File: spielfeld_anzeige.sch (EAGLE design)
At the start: 22 parts, among them IC1 UDN2981A, IC2 UDN2981A, IC3 74HC595N, IC4 74HC595N, IC5 74HC595N

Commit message: Schematic mit 3 Digits fertig
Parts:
- removed R2: (no value), rcl:R-EU_R3216
- JP1: value (none) -> 8 Pin
- L1, L2: value (none) -> red
- R1: value (none) -> 56
- R3: value (none) -> 10k
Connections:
- removed net GND1: C1.2
- removed net GND2: C3.2
- removed net N$18: L2.A, R2.1
- removed net N$19: L1.A, R1.1
- net +5V: now also IC1.VS, IC2.VS; no longer IC1.GND, IC2.GND
- net COLON_OUT: now also IC2.O8, R1.2; no longer RN4D.2
- net GND: now also C1.2, C3.2, IC1.GND, IC2.GND; no longer IC1.VS, IC2.VS, L2.C
- net N$1: now also L1.A, L2.C; no longer ICL1.O1
- net N$13: now also L2.A, R1.1; no longer IC2.O8, RN4D.1
- net R1_OUT: now also D2.R1, D3.R1, ICL1.O1
- net R2_OUT: now also D2.R2, D3.R2, ICL1.O2
- net R3_OUT: now also D2.R3, D3.R3, ICL1.O3
- net R4_OUT: now also D2.R4, D2.R4@1, D3.R4, D3.R4@1, ICL1.O4
- net R5_OUT: now also D2.R5, D3.R5, ICL1.O5
- net R6_OUT: now also D2.R6, D3.R6, ICL1.O6
- net R7_OUT: now also D2.R7, D3.R7, ICL1.O7
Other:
- note added: "Board Connector"
- note added: "Shift-Reg Clear"
- note removed: "Connector"
- moved on the sheet: JP1, L1, L2, R1, R3, RN4D

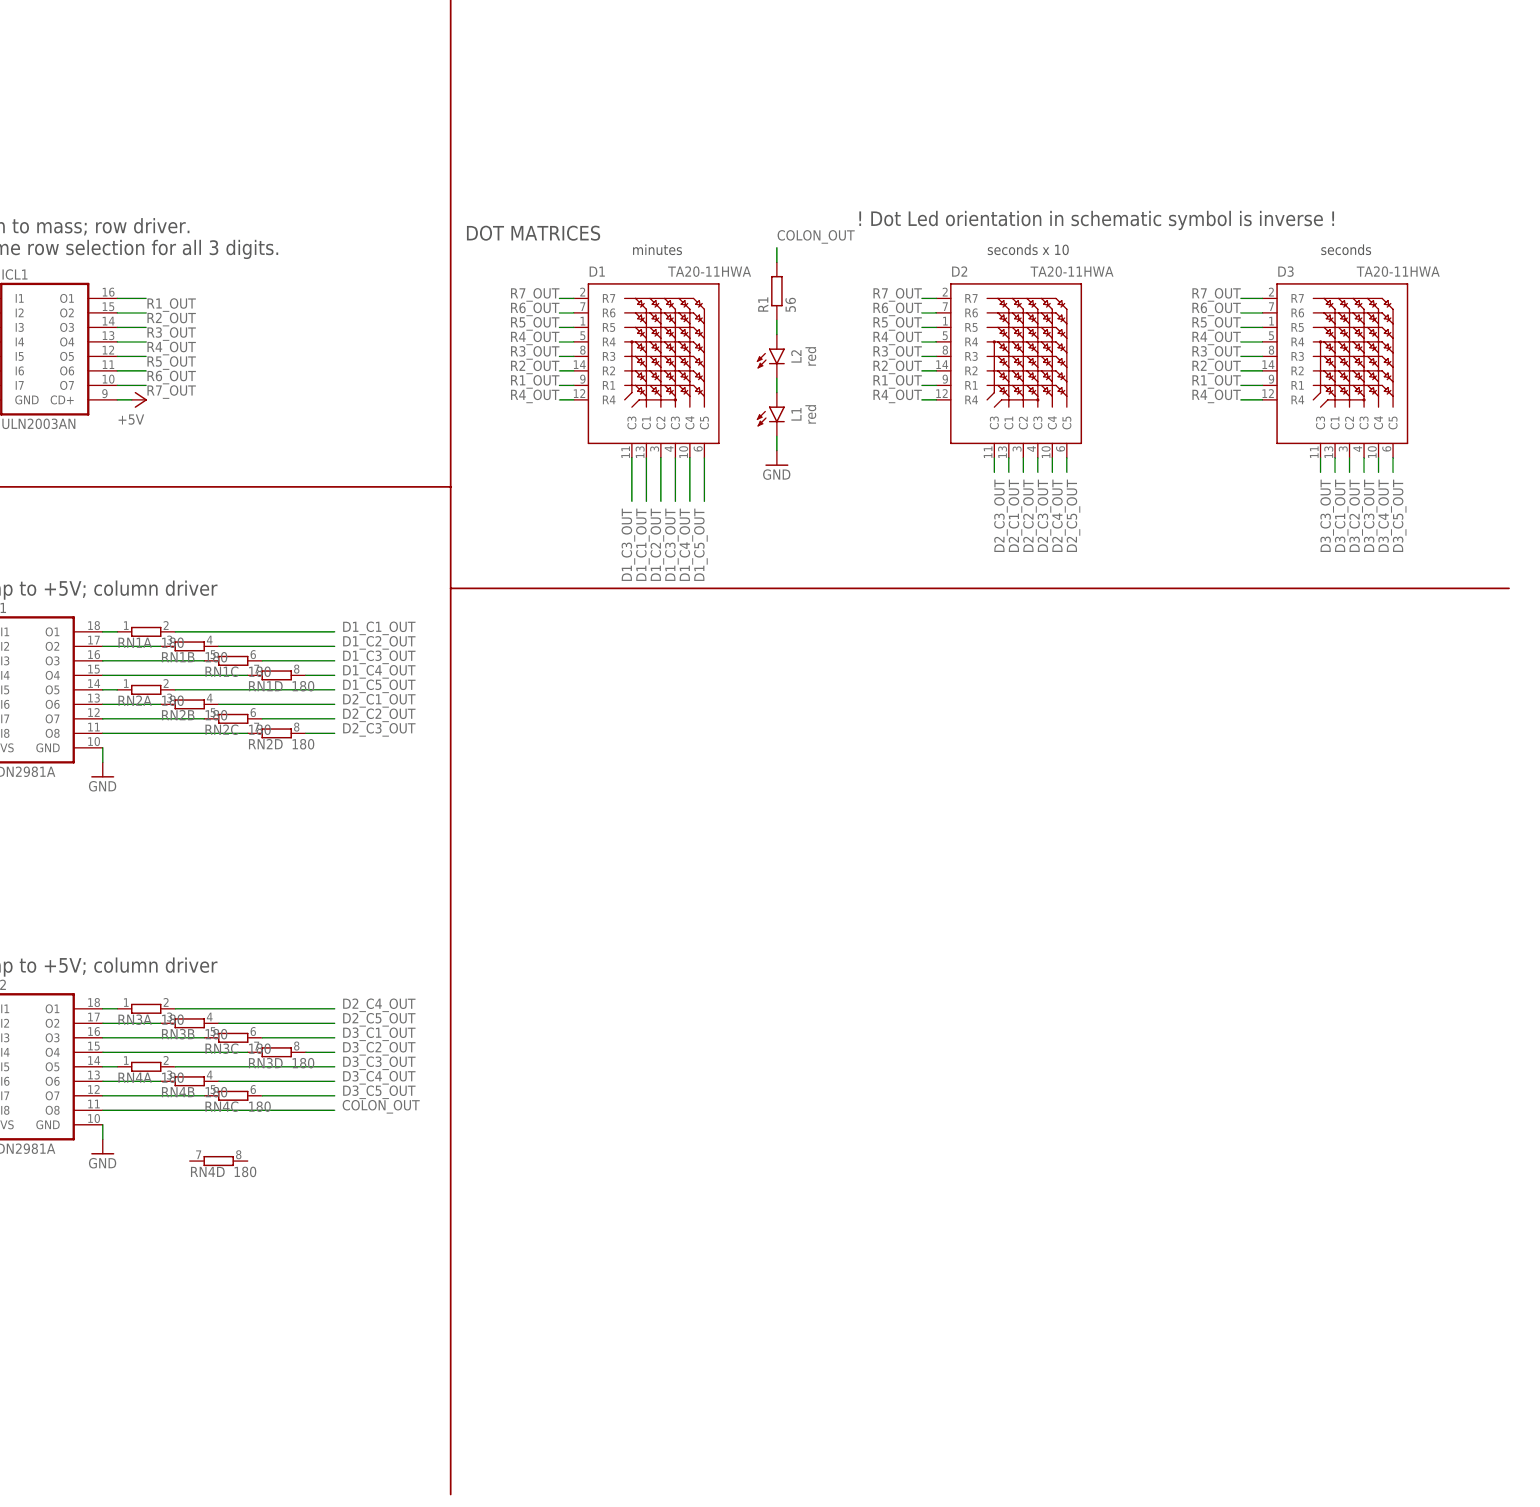
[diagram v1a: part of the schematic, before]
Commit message: Reduced to 2 digits on board. Bom updated.
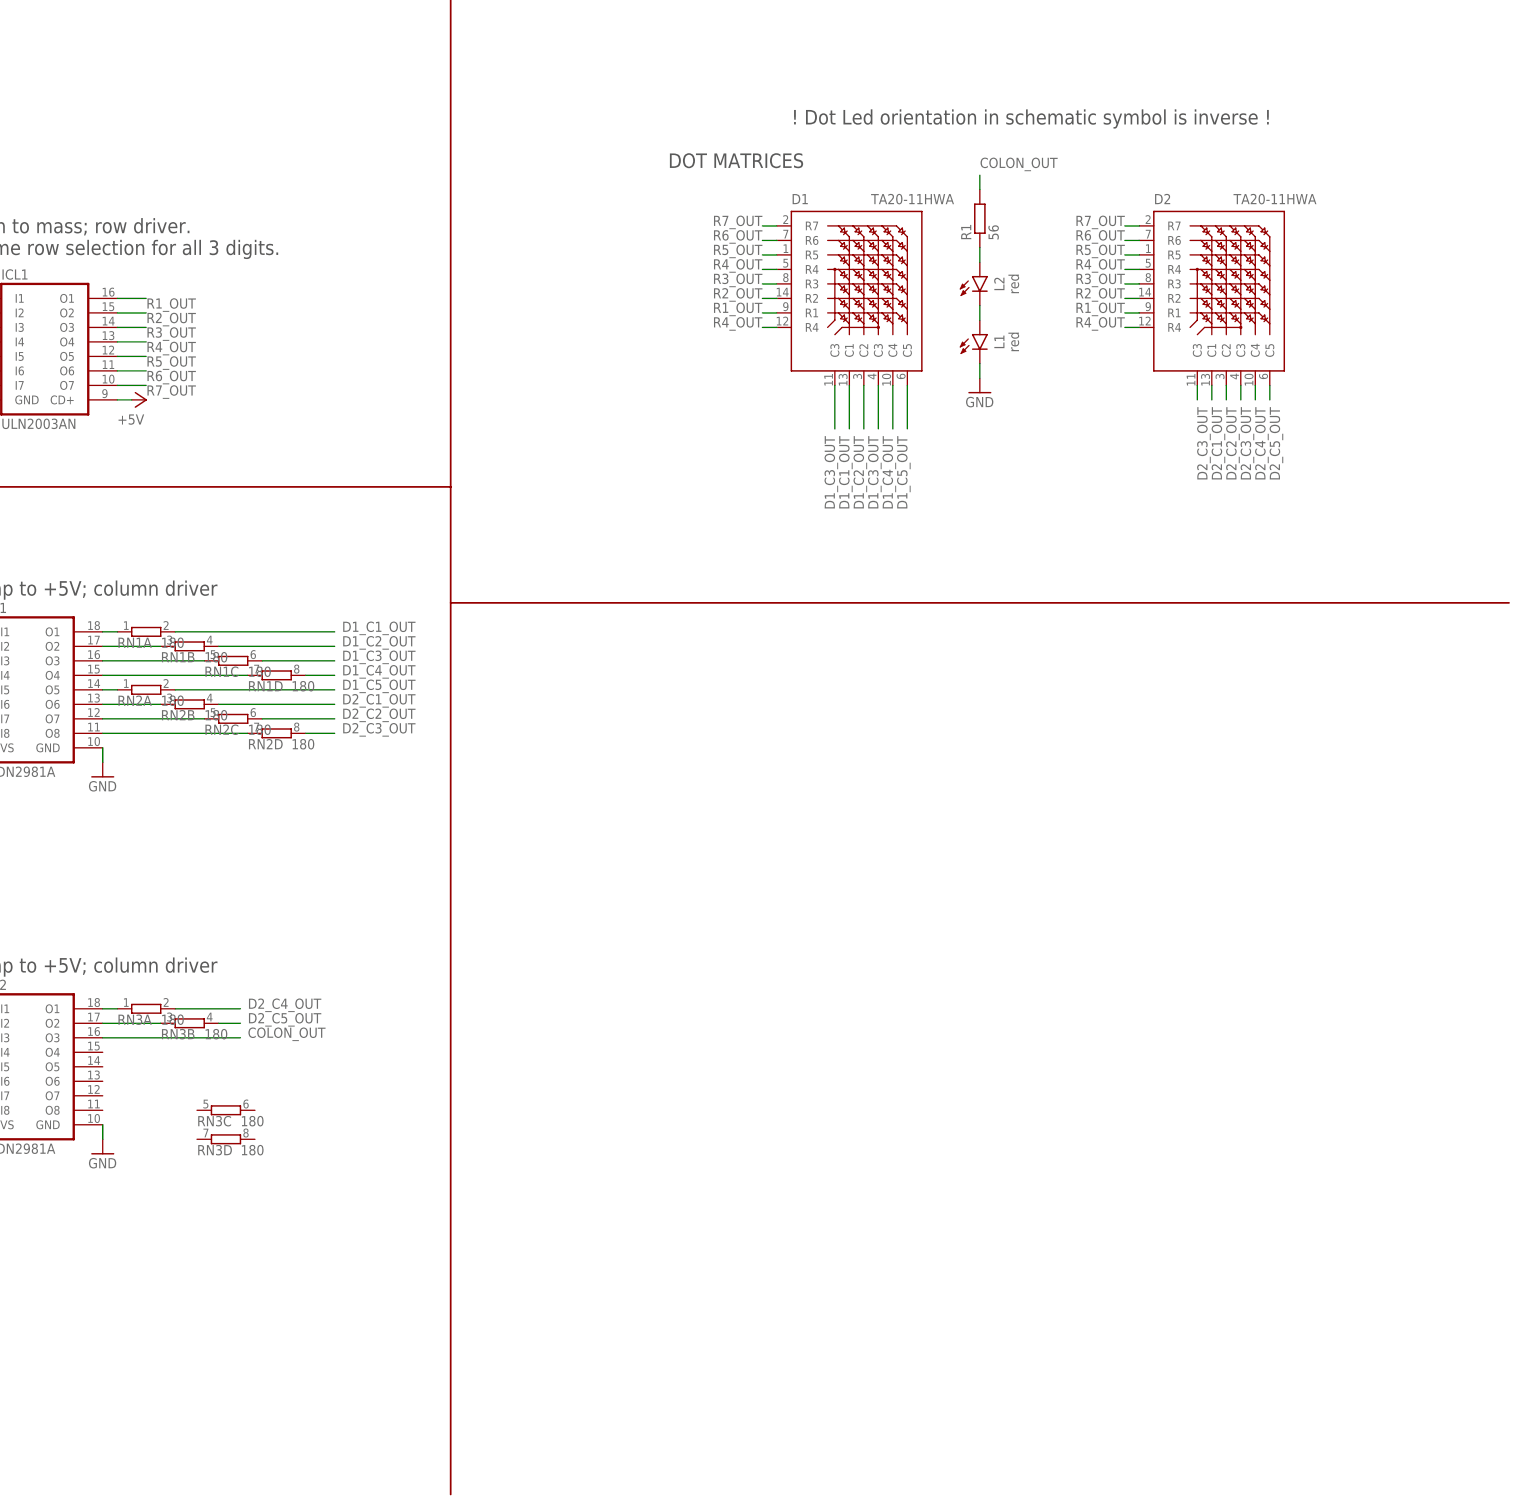
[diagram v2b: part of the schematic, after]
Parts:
- removed D3: TA20-11HWA, display-kingbright:TA20-11HWA
- removed RN4: 180, resistor-sil:E4R
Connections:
- removed net D3_C1_OUT: D3.C1, RN3C.2
- removed net D3_C2_OUT: D3.C2, RN3D.2
- removed net D3_C3_OUT: D3.C3, D3.C3@1, RN4A.2
- removed net D3_C4_OUT: D3.C4, RN4B.2
- removed net D3_C5_OUT: D3.C5, RN4C.2
- removed net N$10: IC2.O5, RN4A.1
- removed net N$11: IC2.O6, RN4B.1
- removed net N$12: IC2.O7, RN4C.1
- removed net N$8: IC2.O3, RN3C.1
- removed net N$9: IC2.O4, RN3D.1
- net COLON_OUT: now also IC2.O3; no longer IC2.O8
- net R1_OUT: no longer D3.R1
- net R2_OUT: no longer D3.R2
- net R3_OUT: no longer D3.R3
- net R4_OUT: no longer D3.R4, D3.R4@1
- net R5_OUT: no longer D3.R5
- net R6_OUT: no longer D3.R6
- net R7_OUT: no longer D3.R7
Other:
- note removed: "minutes"
- note removed: "seconds"
- note removed: "seconds x 10"
- moved on the sheet: D1, D2, L1, L2, R1, RN3C, RN3D

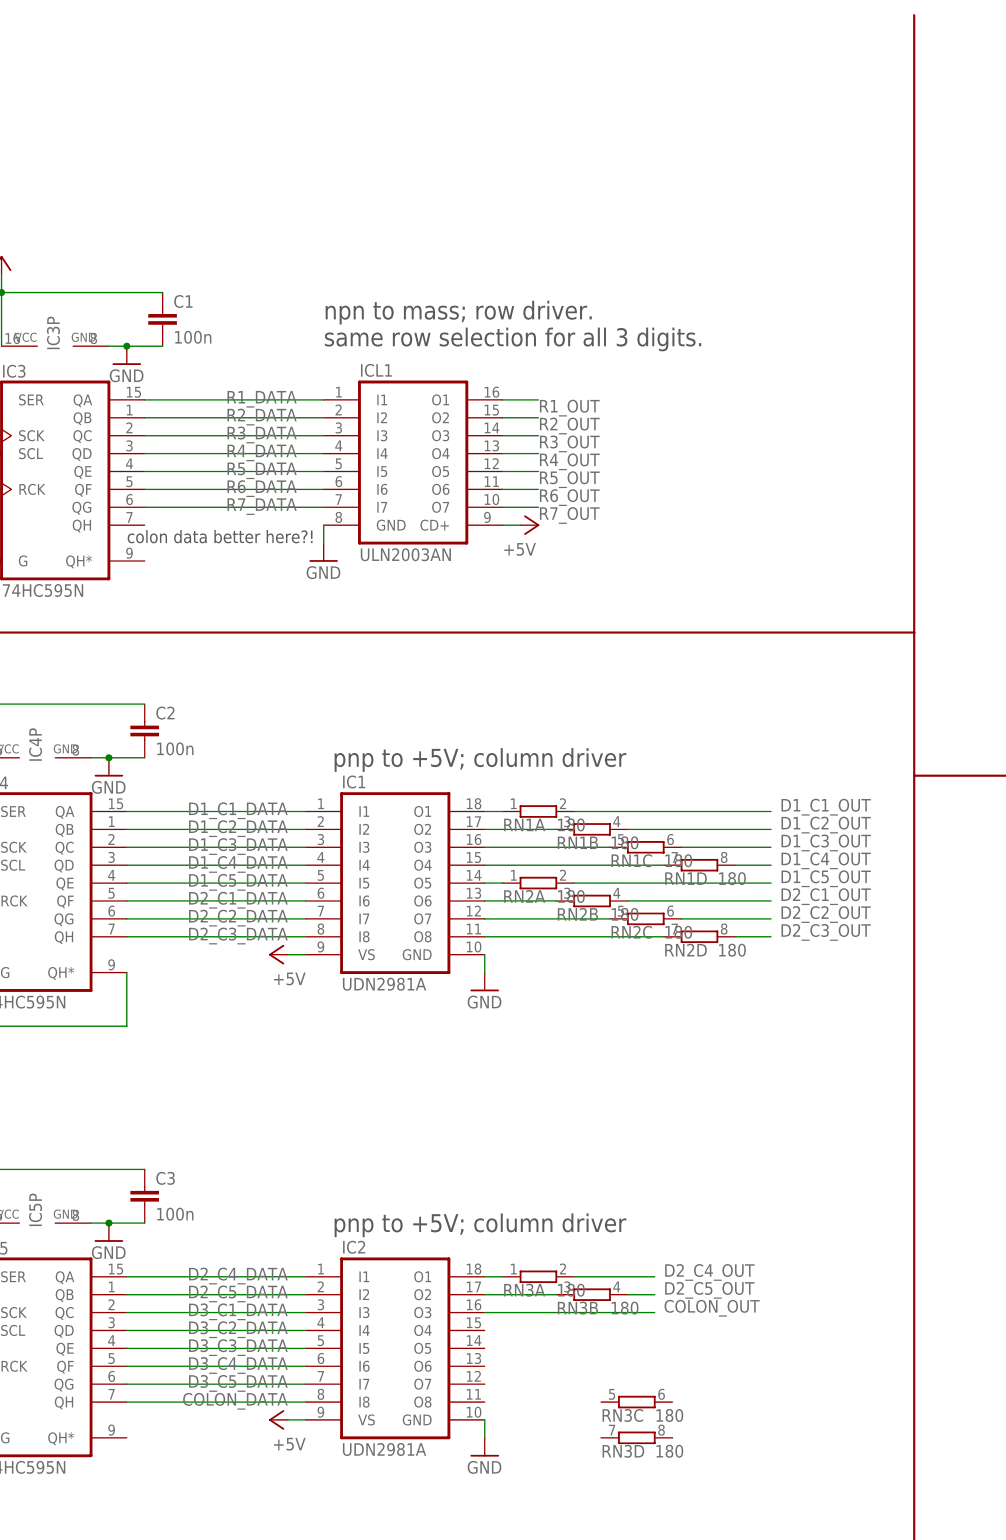
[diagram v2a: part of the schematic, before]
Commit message: PCB design finished with tht parts on backside of board
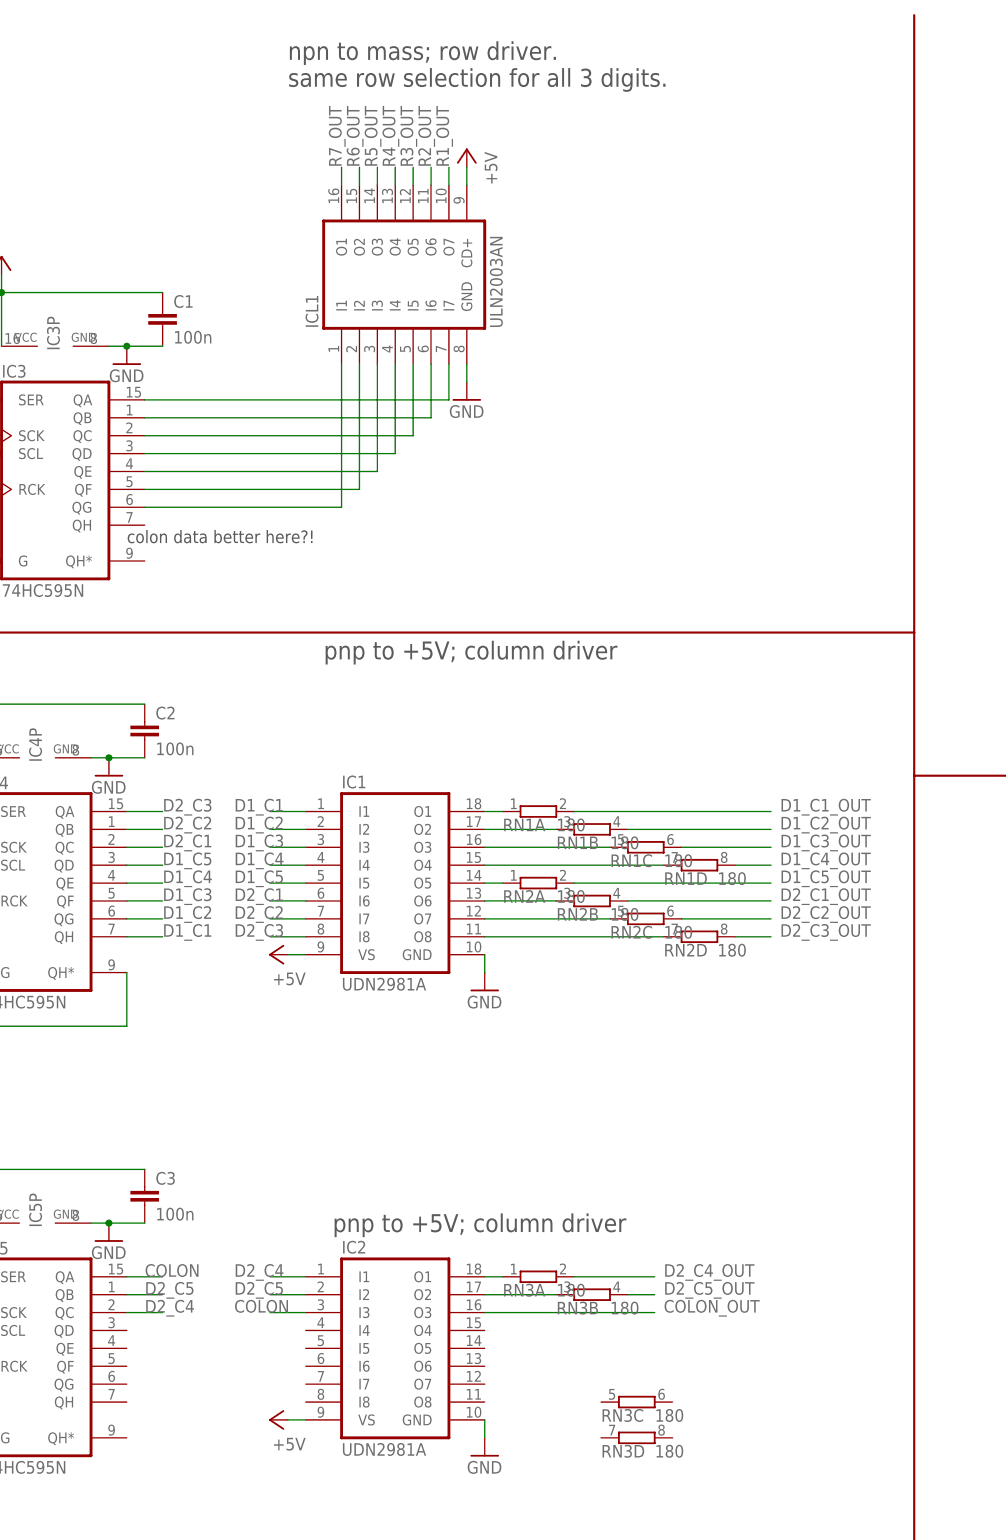
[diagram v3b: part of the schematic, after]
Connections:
- net D2_C5_DATA renamed D2_C5
- net R4_DATA renamed N$11
- removed net COLON_DATA: IC2.I8, IC5A.QH
- removed net D1_C1_DATA: IC1.I1, IC4A.QA
- removed net D1_C2_DATA: IC1.I2, IC4A.QB
- removed net D1_C3_DATA: IC1.I3, IC4A.QC
- removed net D1_C4_DATA: IC1.I4, IC4A.QD
- removed net D1_C5_DATA: IC1.I5, IC4A.QE
- removed net D2_C1_DATA: IC1.I6, IC4A.QF
- removed net D2_C2_DATA: IC1.I7, IC4A.QG
- removed net D2_C3_DATA: IC1.I8, IC4A.QH
- removed net D2_C4_DATA: IC2.I1, IC5A.QA
- removed net D3_C1_DATA: IC2.I3, IC5A.QC
- removed net D3_C2_DATA: IC2.I4, IC5A.QD
- removed net D3_C3_DATA: IC2.I5, IC5A.QE
- removed net D3_C4_DATA: IC2.I6, IC5A.QF
- removed net D3_C5_DATA: IC2.I7, IC5A.QG
- removed net R1_DATA: IC3A.QA, ICL1.I1
- removed net R2_DATA: IC3A.QB, ICL1.I2
- removed net R3_DATA: IC3A.QC, ICL1.I3
- removed net R5_DATA: IC3A.QE, ICL1.I5
- removed net R6_DATA: IC3A.QF, ICL1.I6
- removed net R7_DATA: IC3A.QG, ICL1.I7
- new net COLON: IC2.I3, IC5A.QA
- new net D1_C1: IC1.I1, IC4A.QH
- new net D1_C2: IC1.I2, IC4A.QG
- new net D1_C3: IC1.I3, IC4A.QF
- new net D1_C4: IC1.I4, IC4A.QE
- new net D1_C5: IC1.I5, IC4A.QD
- new net D2_C1: IC1.I6, IC4A.QC
- new net D2_C2: IC1.I7, IC4A.QB
- new net D2_C3: IC1.I8, IC4A.QA
- new net D2_C4: IC2.I1, IC5A.QC
- new net N$10: IC3A.QC, ICL1.I5
- new net N$12: IC3A.QE, ICL1.I3
- new net N$18: IC3A.QF, ICL1.I2
- new net N$21: IC3A.QG, ICL1.I1
- new net N$8: IC3A.QA, ICL1.I7
- new net N$9: IC3A.QB, ICL1.I6
- net R1_OUT: now also ICL1.O7; no longer ICL1.O1
- net R2_OUT: now also ICL1.O6; no longer ICL1.O2
- net R3_OUT: now also ICL1.O5; no longer ICL1.O3
- net R5_OUT: now also ICL1.O3; no longer ICL1.O5
- net R6_OUT: now also ICL1.O2; no longer ICL1.O6
- net R7_OUT: now also ICL1.O1; no longer ICL1.O7
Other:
- moved on the sheet: ICL1
